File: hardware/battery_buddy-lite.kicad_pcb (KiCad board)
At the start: 2 copper layers, 75 x 50.8 mm, 62 parts, among them J1 USB_C_Receptacle_USB2.0_16P, J2 BM04B-SRSS-TB, J3 Conn_01x10_MountingPin, J4 S4B-PH-SM4-TB, J5 Conn_01x01, SW1 SW_Push, U1 USBLC6-2P6, U2 LTC2959IDDB, U3 SN65HVD230DR, U4 ESP32-C3-MINI-1-N4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

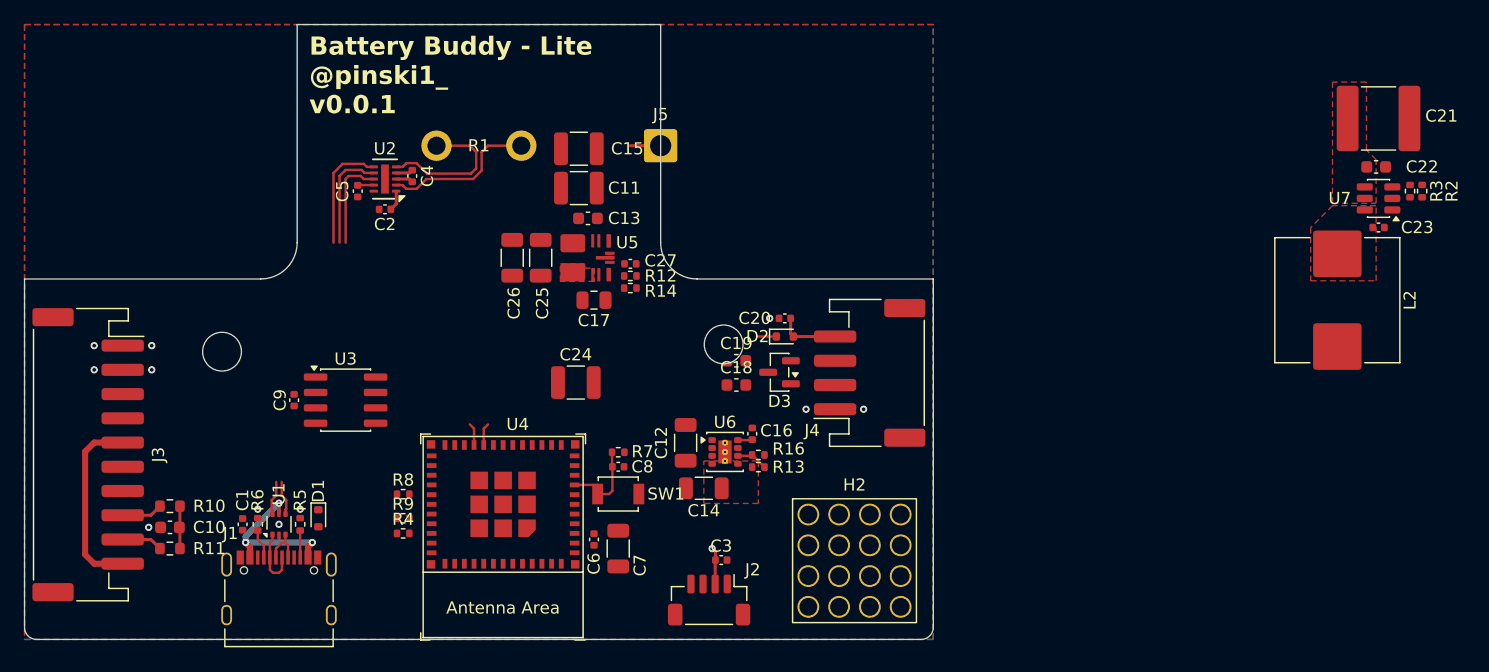
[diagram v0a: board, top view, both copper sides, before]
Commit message: masking pin 11 of LTC2959
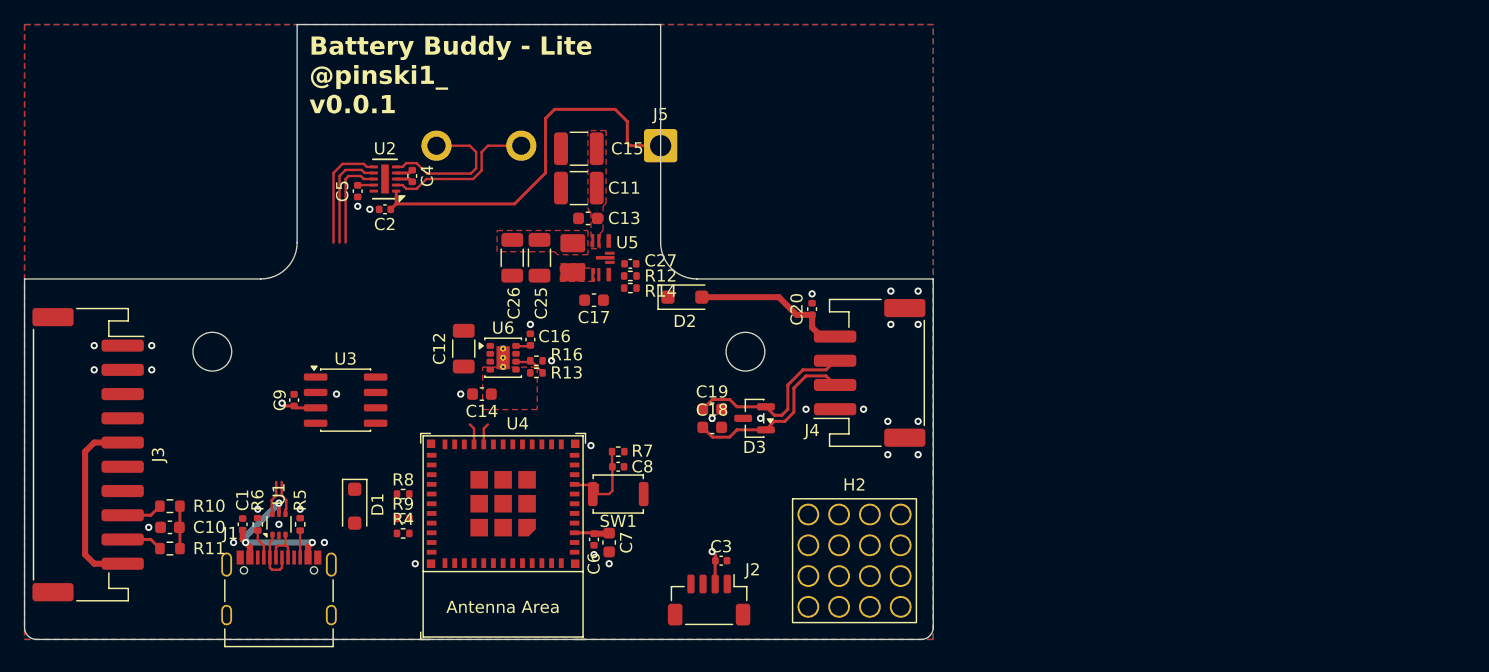
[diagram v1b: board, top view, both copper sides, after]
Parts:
- removed C21: 4.7uF 100V, Capacitor_SMD:C_2220_5750Metric
- removed C22: 100nF 100V, Capacitor_SMD:C_0603_1608Metric
- removed C23: 100nF, Capacitor_SMD:C_0402_1005Metric
- removed C24: 22uF 25V, Capacitor_SMD:C_1210_3225Metric
- removed L2: 56uH 2.0A, Inductor_SMD:L_Wuerth_HCI-1050
- removed R2: 100k, Resistor_SMD:R_0402_1005Metric
- removed R3: 7.15k, Resistor_SMD:R_0402_1005Metric
- removed U7: LMR51610XDBVR, Package_TO_SOT_SMD:SOT-23-6
- C10: value 47nF -> 4.7nF
- C12: value 10uF -> 10uF 25V
- C14, C7: value 10uF -> 10uF 6.3V; footprint Capacitor_SMD:C_1206_3216Metric -> Capacitor_SMD:C_0603_1608Metric
- C17: footprint Capacitor_SMD:C_0805_2012Metric -> Capacitor_SMD:C_0603_1608Metric
- D1, D2: value D_Schottky -> DSK14; footprint Diode_SMD:D_SOD-523 -> Diode_SMD:D_SOD-123F
- D3: value NUP2105L -> NUP2105LT1G
- J2: value BM04B-SRSS-TB -> BM04B-SRSS-TB(LF)(SN)
- J3: value Conn_01x10_MountingPin -> S10B-PH-SM4-TB(LF)(SN)
- R1: value CSM2F-6918-L050J30 -> ARCS6918JL050A9; moved to B.Cu
- SW1: value SW_Push -> SPST; footprint Button_Switch_SMD:SW_SPST_B3U-1000P -> Button_Switch_SMD:SW_Push_SPST_NO_Alps_SKRK
- moved C12 19.9 mm to (148.8, 91.8)
- moved C14 19.9 mm to (150.2, 95.5)
- moved C16 19.9 mm to (154.2, 91.0)
- moved R13 19.9 mm to (154.8, 93.8)
- moved R16 19.9 mm to (154.8, 92.8)
- moved U6 19.9 mm to (152.0, 92.5)
- moved D2 8.87 mm to (167.0, 87.5)
- moved C19 4.47 mm to (169.2, 96.8)
- moved D3 4.32 mm to (172.8, 97.5)
- moved C18 4.03 mm to (169.2, 98.2)
- moved D1 3.16 mm to (139.8, 104.8)
- moved C20 2.38 mm to (177.5, 88.5), turned to 90 degrees
- moved H3 1.90 mm to (172.0, 92.0)
- moved C7 0.90 mm to (160.8, 107.8)
- moved H1 0.80 mm to (128.0, 92.0)
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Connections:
- C20 pad 1: unconnected-(C20-Pad1) -> Net-(D2-A)
- D2 pad 2: unconnected-(C20-Pad1) -> Net-(D2-A)
- J4 pad 4: unconnected-(C20-Pad1) -> Net-(D2-A)
- U4 pad 20: /CAN_RX -> /CAN_2_MCU
- U4 pad 21: /CAN_TX -> /MCU_2_CAN
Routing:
- net VCC: track 4.18 -> 31.6 mm
- net /CAN_L: track 0.00 -> 14.8 mm
- net /CAN_H: track 0.00 -> 14.8 mm
- net Net-(D2-A): track 0.00 -> 13.0 mm
- net +3V3: track 3.05 -> 8.88 mm, vias 1 -> 2
- net unconnected-(C20-Pad1): track 5.04 -> 0.00 mm
- net /MCU_2_CAN: track 0.00 -> 1.84 mm
- net /CAN_TX: track 1.84 -> 0.00 mm
- net /CAN_RX: track 1.84 -> 0.00 mm
- net /CAN_2_MCU: track 0.00 -> 1.84 mm
- net +12V: track 16.9 -> 15.3 mm
- net /VBUS: track 13.5 -> 14.6 mm
- net GND: vias 11 -> 33
- added copper zone on F.Cu, net +12V
- removed copper zone on F.Cu, net Net-(U7-SW)
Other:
- board text added: "0.2000 mm / 0.2000 mm"
- board text added: "0.3000 mm"
- board text added: "1.6000 mm"
- board text added: "2"
- board text added: "75.0000 mm x 50.7500 mm"
- board text added: "BOARD CHARACTERISTICS"
- board text added: "Board Thickness:"
- board text added: "Board overall dimensions:"
- board text added: "Castellated pads:"
- board text added: "Copper Finish:"
- board text added: "Copper Layer Count:"
- board text added: "Edge card connectors:"
- board text added: "Impedance Control:"
- board text added: "Min hole diameter:"
- board text added: "Min track/spacing:"
- board text added: "No"
- board text added: "None"
- board text added: "Plated Board Edge:"

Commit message: updating board shape and USB C conn
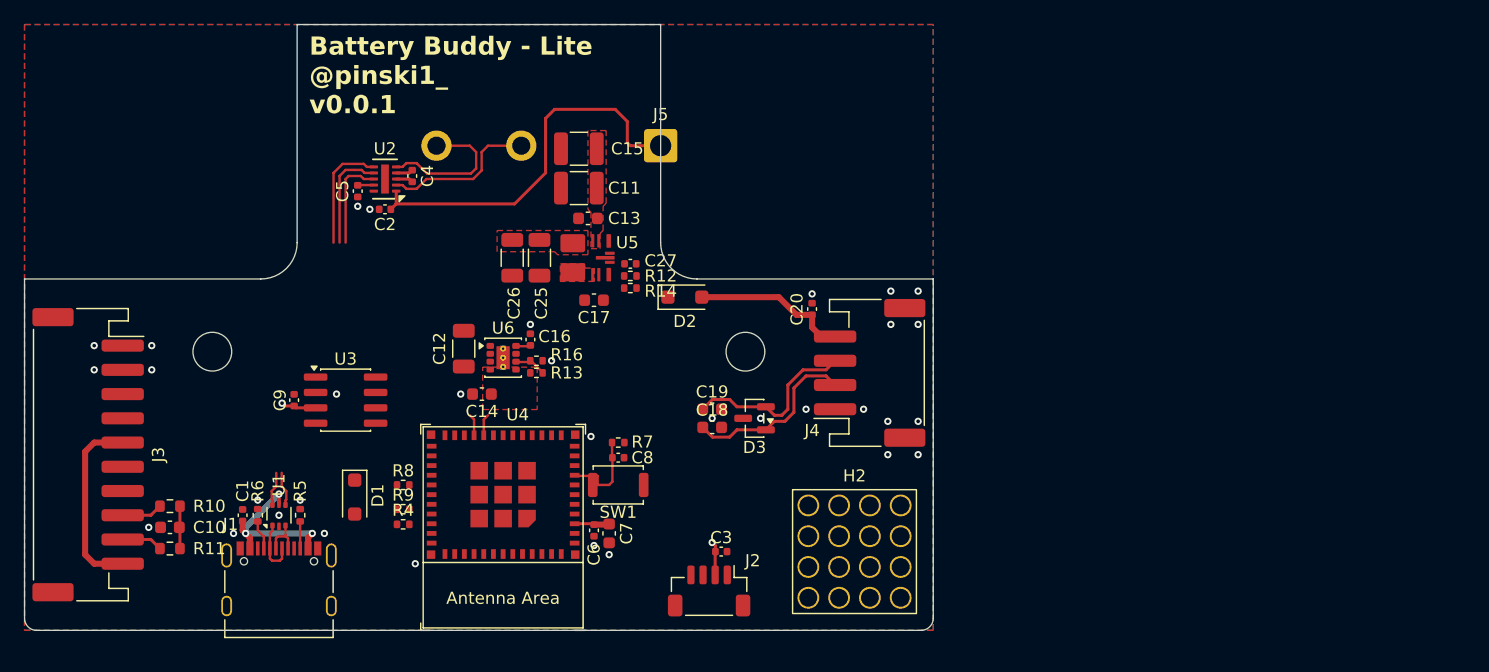
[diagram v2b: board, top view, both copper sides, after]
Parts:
- moved C1 0.75 mm to (130.5, 105.5)
- moved C3 0.75 mm to (170.0, 108.5)
- moved C6 0.75 mm to (159.5, 106.8)
- moved C7 0.75 mm to (160.8, 107.0)
- moved C8 0.75 mm to (161.5, 100.8)
- moved D1 0.75 mm to (139.8, 104.0)
- moved H2 0.75 mm to (181.0, 108.5)
- moved J1 0.75 mm to (133.5, 110.8)
- moved J2 0.75 mm to (169.0, 111.8)
- moved R4 0.75 mm to (143.8, 106.2)
- moved R5 0.75 mm to (135.2, 105.5)
- moved R6 0.75 mm to (131.8, 105.5)
- moved R7 0.75 mm to (161.5, 99.5)
- moved R8 0.75 mm to (143.8, 103.0)
- moved R9 0.75 mm to (143.8, 105.0)
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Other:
- board size 75 x 50.8 mm -> 75 x 50 mm
